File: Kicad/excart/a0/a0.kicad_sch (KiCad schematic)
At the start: 7 parts, among them J1 Conn_02x17_Odd_Even, U1 SST39SF040, U2 74LS174, U3 74HC138

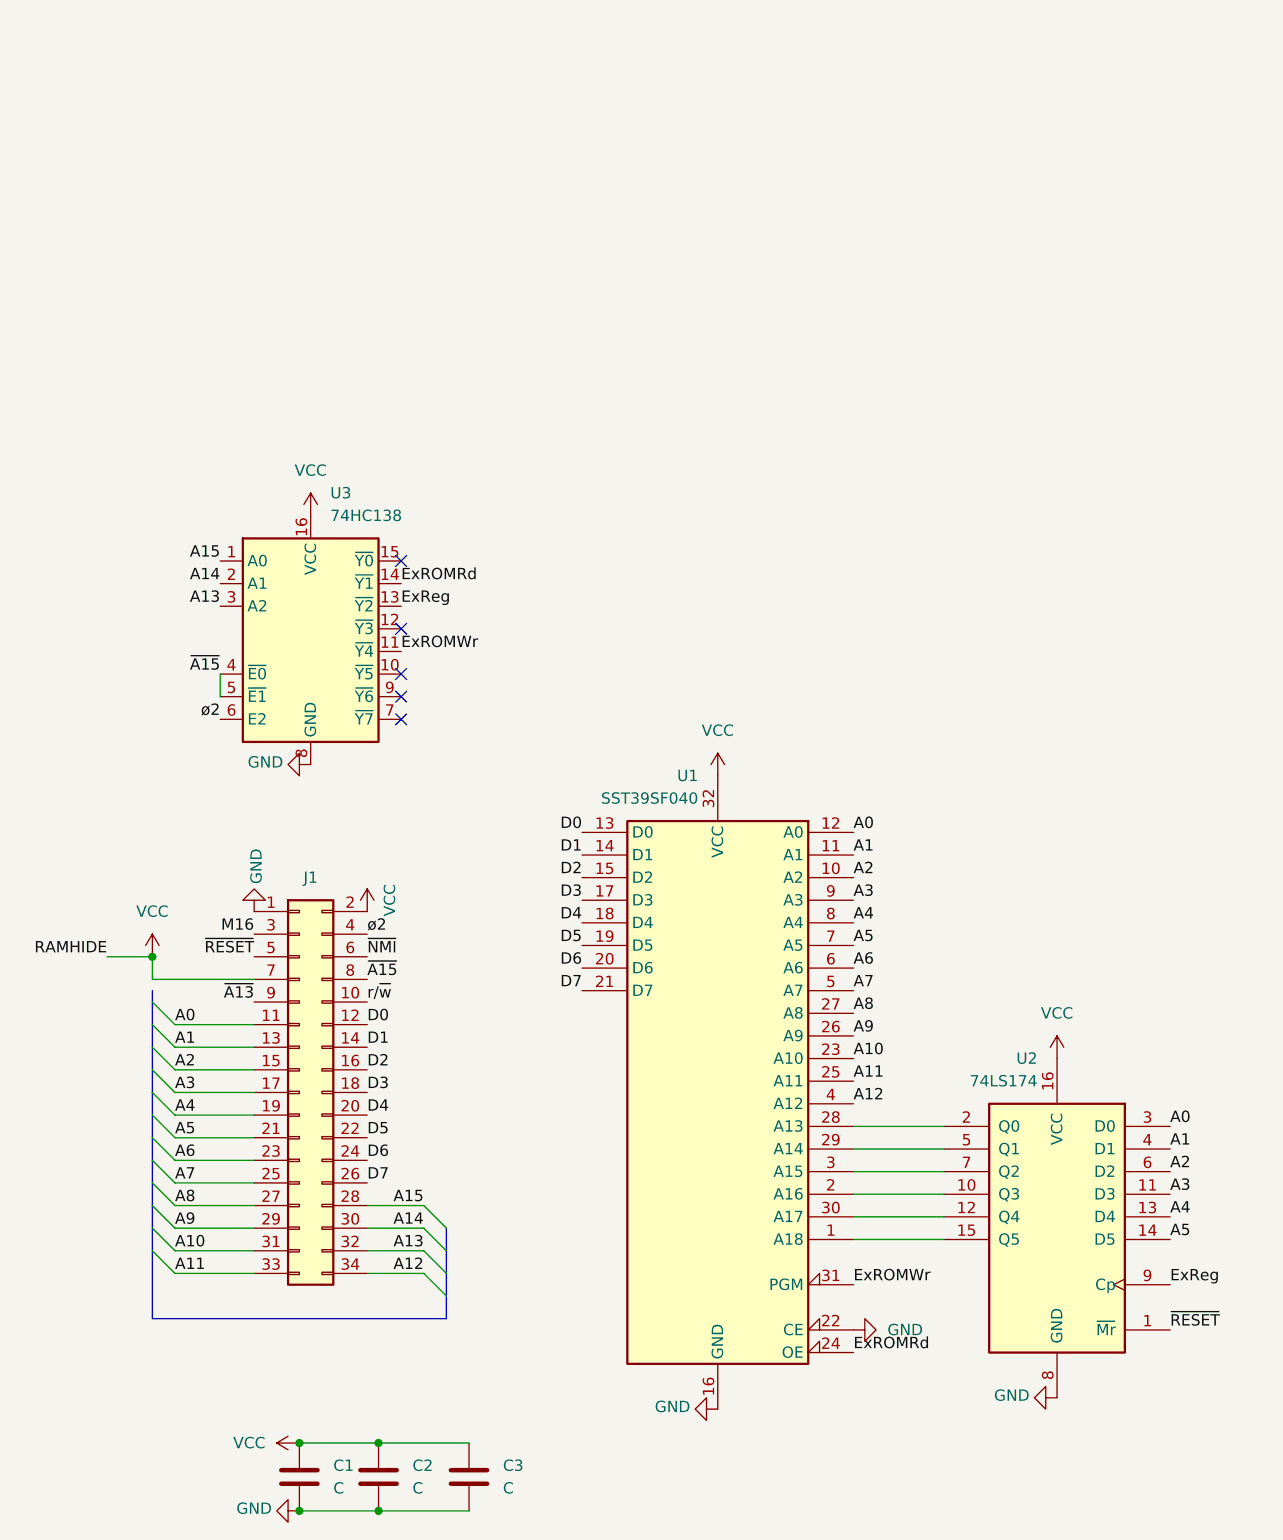
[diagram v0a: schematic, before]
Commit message: Add TTL/MIC level jumper to trs jack
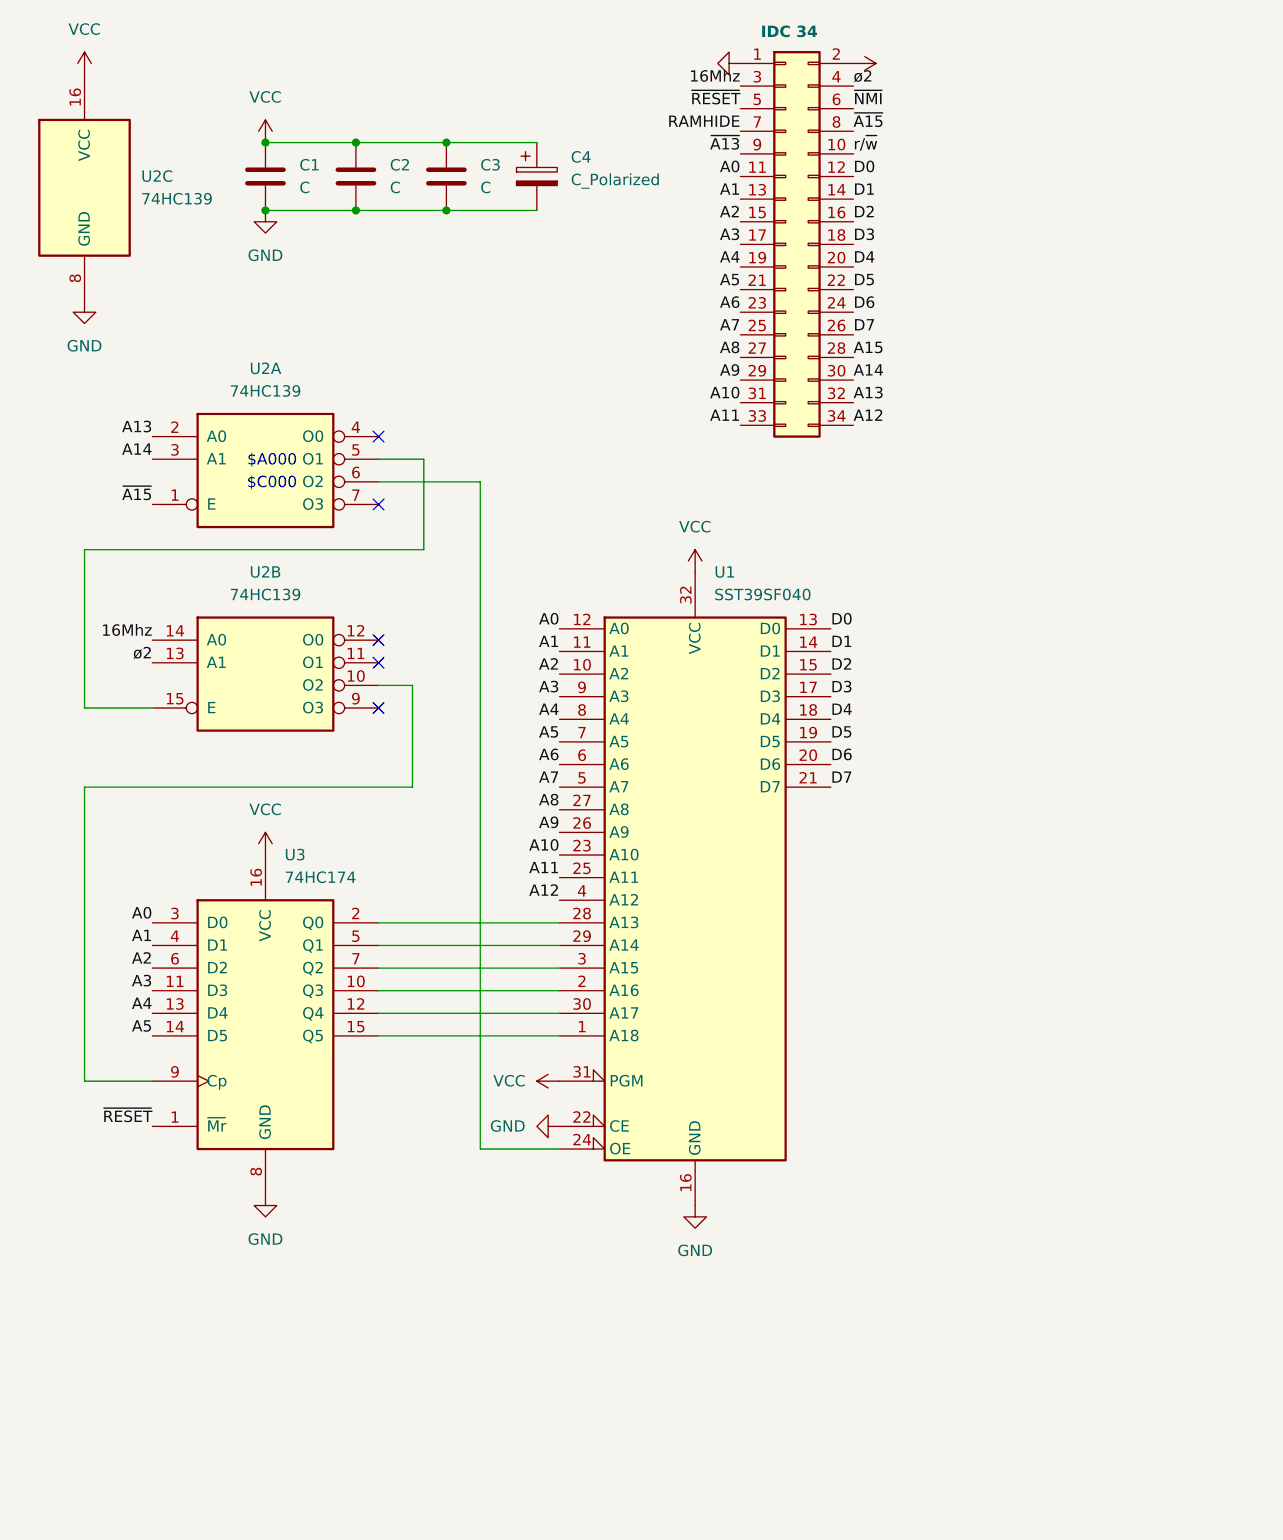
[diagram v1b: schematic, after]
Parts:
- removed U2: 74LS174, PCM_Package_DIP_AKL:DIP-16_W7.62mm_LongPads, symbol 74xx:74LS174
- removed U3: 74HC138, PCM_Package_DIP_AKL:DIP-16_W7.62mm_LongPads, symbol 74xx:74HC138
- added C4: C_Polarized, Capacitor_THT:CP_Radial_D5.0mm_P2.50mm, symbol Device:C_Polarized
- added U2: 74HC139, Package_DIP:DIP-16_W7.62mm, symbol 74xx_ALT:74HC139
- added U3: 74HC174, Package_DIP:DIP-16_W7.62mm, symbol 74xx:74LS174
- J1: value Conn_02x17_Odd_Even -> IDC 34; footprint Connector_IDC:IDC-Header_2x17_P2.54mm_Horizontal -> Connector_PinSocket_2.54mm:PinSocket_2x17_P2.54mm_Vertical
- U1: footprint Package_DIP:DIP-32_W15.24mm_LongPads -> Global:PLCC-DIP-32_THT-Socket
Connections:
- net ExROMWr is gone; now on net VCC: U1.31 (PGM)
- net A0: now also U3.3 (D0)
- net A1: now also U3.4 (D1)
- net A13: now also U2.2 (A0)
- net A14: now also U2.3 (A1)
- net A2: now also U3.6 (D2)
- net A3: now also U3.11 (D3)
- net A4: now also U3.13 (D4)
- net A5: now also U3.14 (D5)
- net GND: now also C1.2, C2.2, C3.2, C4.2, U2.8 (GND), U3.8 (GND); no longer C1.1, C2.1, C3.1
- net VCC: now also C1.1, C2.1, C3.1, C4.1, U2.16 (VCC), U3.16 (VCC); no longer C1.2, C2.2, C3.2, J1.7 (Pin_7)
- net ~{A15}: now also U2.1 (E)
- net ~{RESET}: now also U3.1 (~{Mr})
- net ø2: now also U2.13 (A1)
- net at U1.2 (A16): now also U3.10 (Q3)
- net at U1.30 (A17): now also U3.12 (Q4)
- net at U1.1 (A18): now also U3.15 (Q5)
- net at U1.28 (A13): now also U3.2 (Q0)
- net at U1.29 (A14): now also U3.5 (Q1)
- net at U1.3 (A15): now also U3.7 (Q2)
- net ExROMRd: no longer names the net of U1.24 (OE)
- net ExROMRd: now also U2.6 (O2)
- net M16 renamed 16Mhz
- net 16Mhz: now also U2.14 (A0)
- new net: U2.15 (E), U2.5 (O1)
- new net: U2.10 (O2), U3.9 (Cp)
- new net RAMHIDE: J1.7 (Pin_7)
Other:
- note added: "$A000"
- note added: "$C000"
- title: (none) -> MicroMicro 512KiB Expansion Cart
